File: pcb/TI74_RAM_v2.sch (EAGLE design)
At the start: 11 parts, among them IC1 JEDEC_32KB_SRAM, X1 TI74_CONN

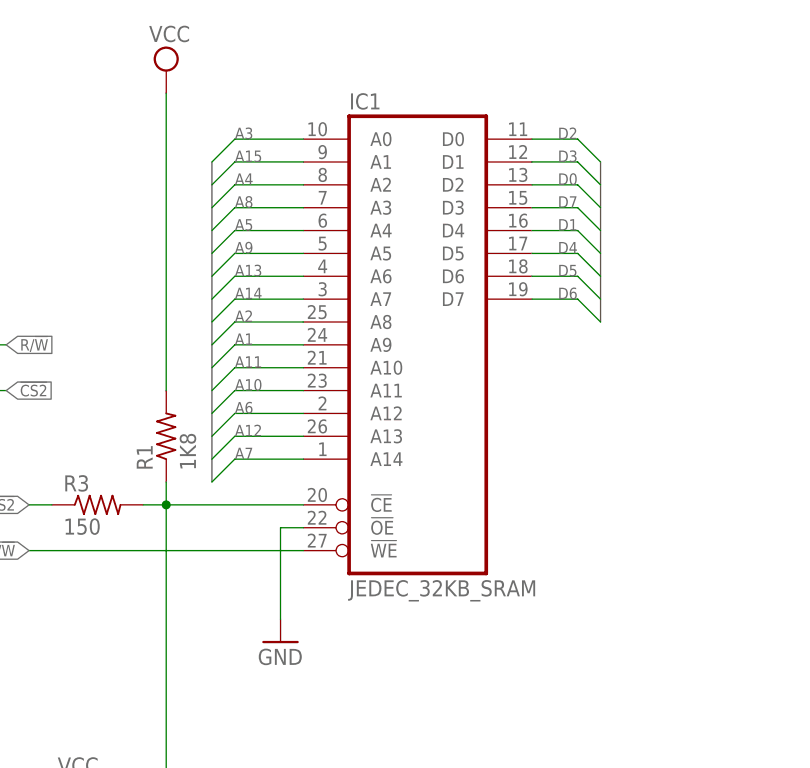
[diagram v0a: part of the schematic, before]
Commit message: Fixed A15->A0 mistake and shortened board (v2)
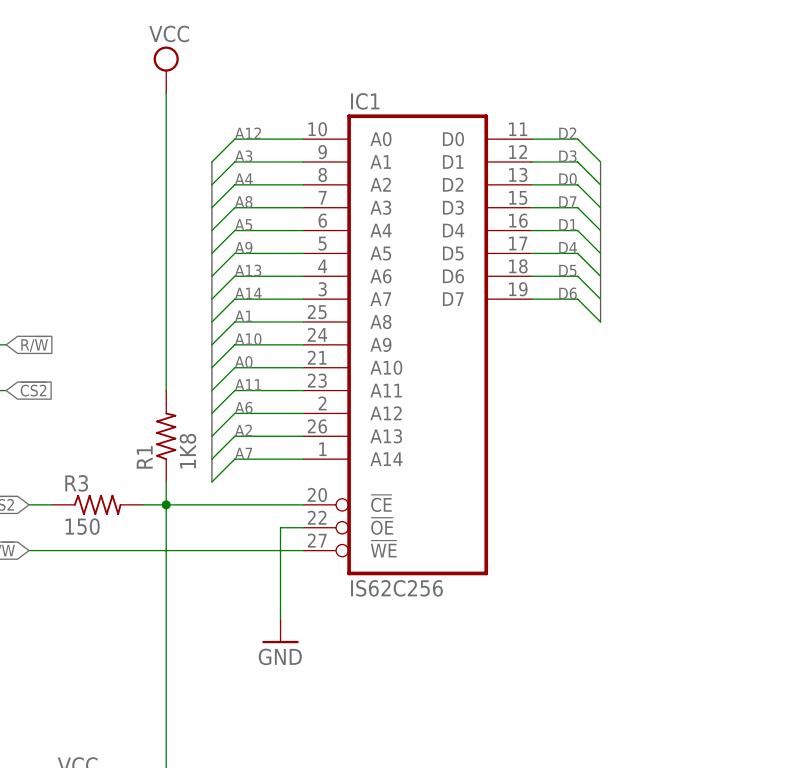
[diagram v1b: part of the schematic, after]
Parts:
- IC1: value JEDEC_32KB_SRAM -> IS62C256
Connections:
- net A0: now also IC1A.A10
- net A1: now also IC1A.A8; no longer IC1A.A9
- net A10: now also IC1A.A9; no longer IC1A.A11
- net A11: now also IC1A.A11; no longer IC1A.A10
- net A12: now also IC1A.A0; no longer IC1A.A13
- net A15: no longer IC1A.A1
- net A2: now also IC1A.A13; no longer IC1A.A8
- net A3: now also IC1A.A1; no longer IC1A.A0
